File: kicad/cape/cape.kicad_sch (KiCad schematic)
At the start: 15 parts, among them M1 Motor_Servo_Feedback, M2 Motor_Servo_Feedback, P8 BeagleBone_Black_Header, P9 BeagleBone_Black_Header, U1 BNO055, U2 S13V20F5

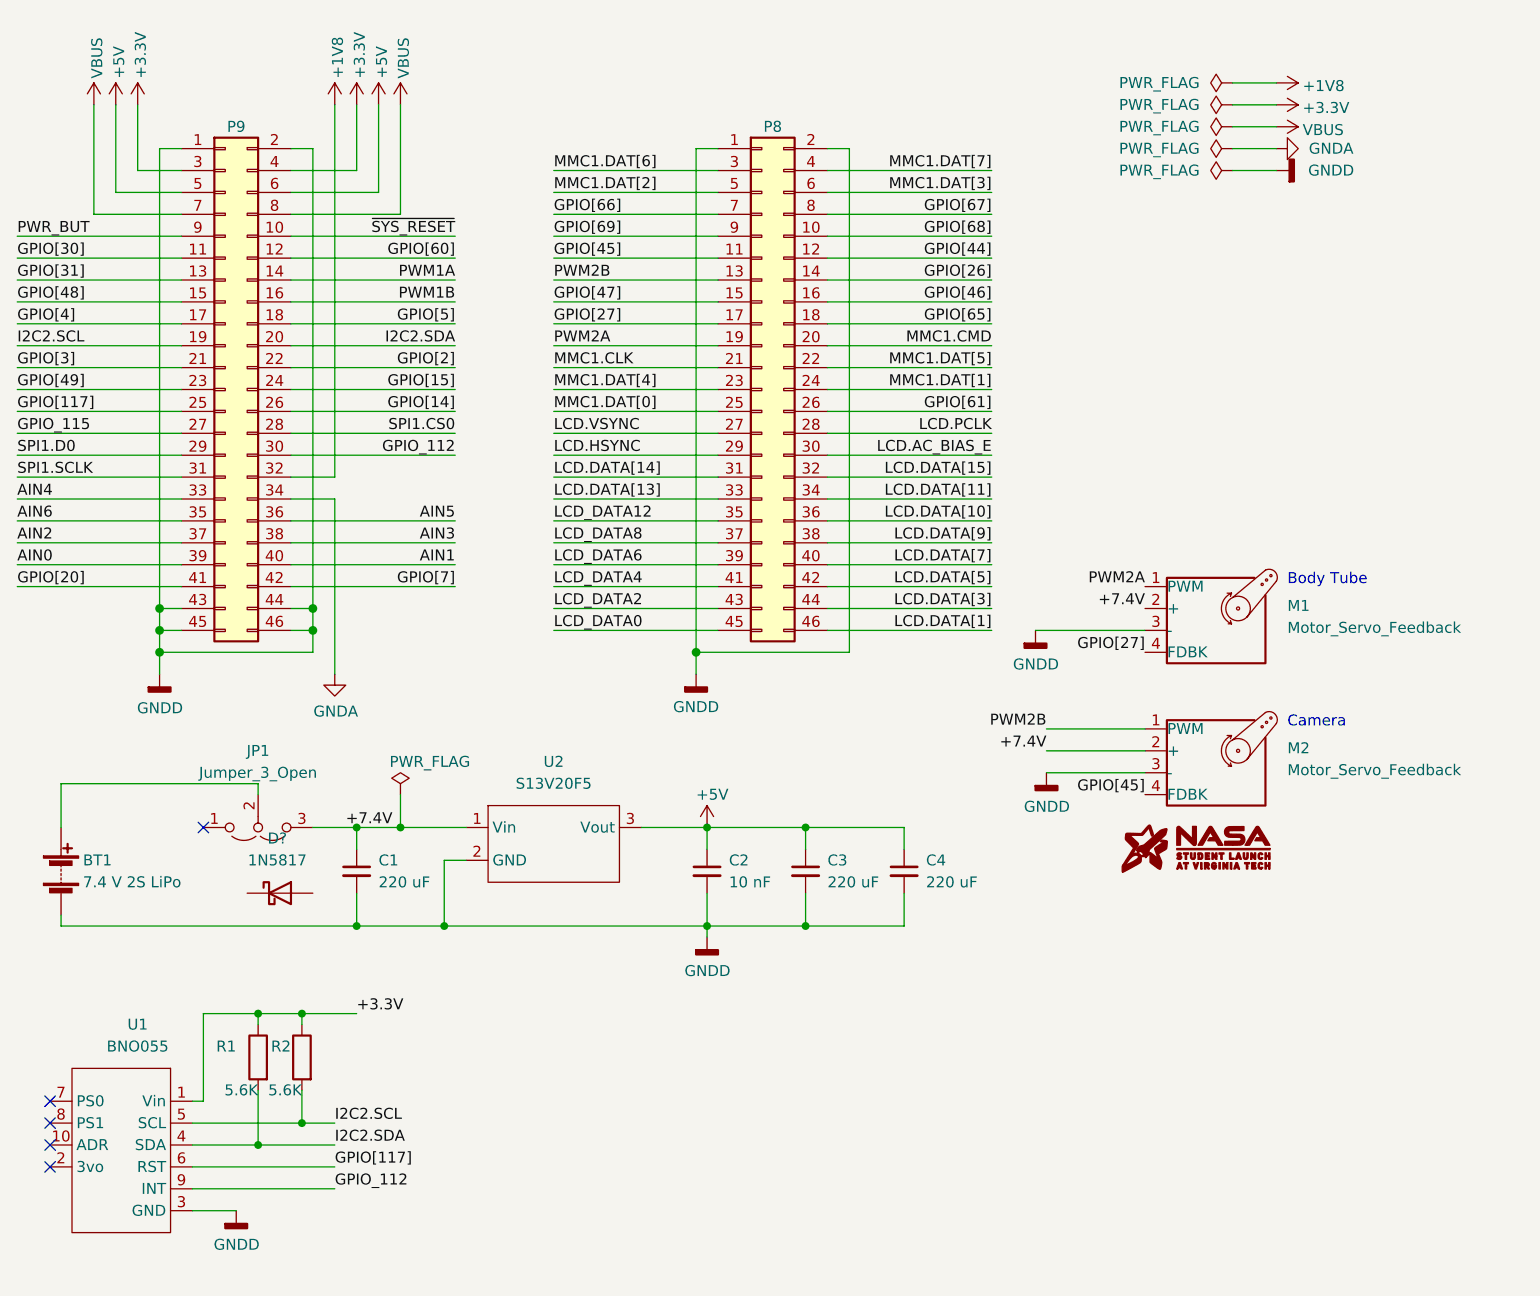
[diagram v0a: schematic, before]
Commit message: Finished schematic v1-5
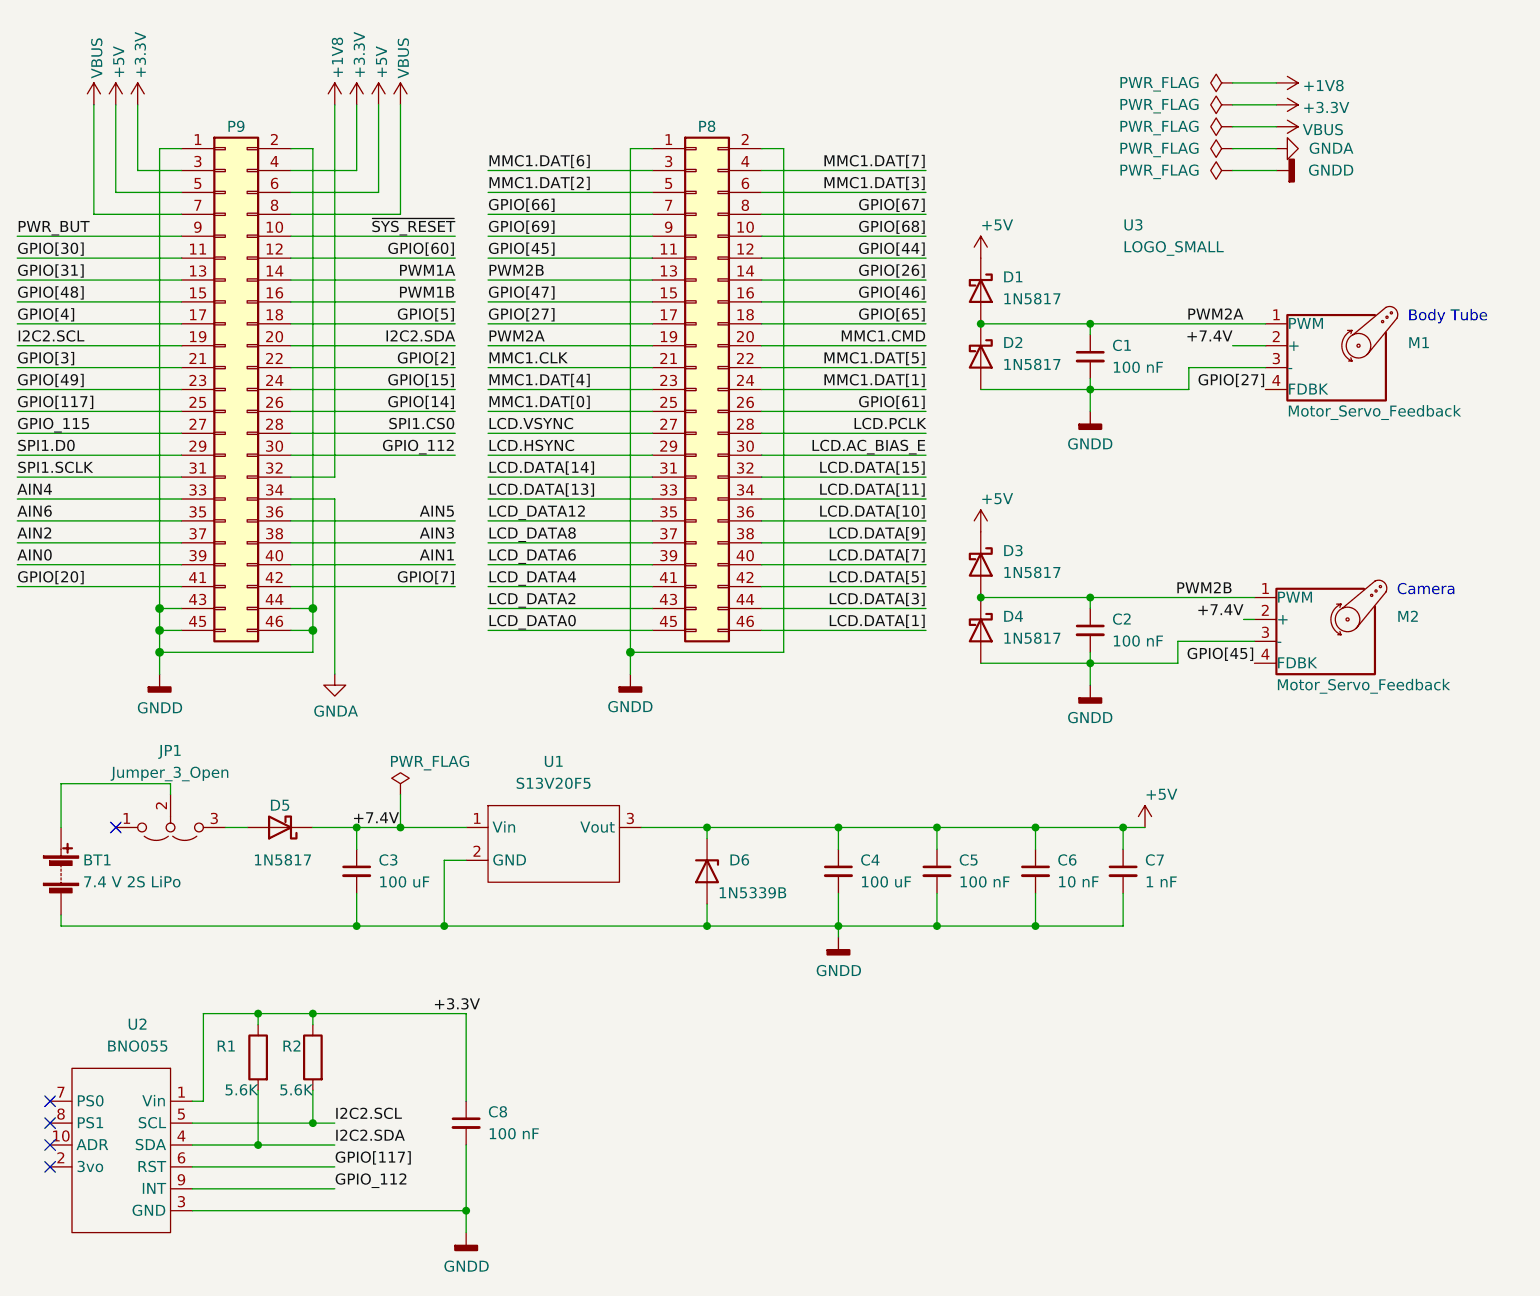
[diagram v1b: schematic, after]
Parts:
- removed C3: 220 uF, Capacitor_THT:C_Radial_D8.0mm_H7.0mm_P3.50mm, symbol Device:C_Small
- added C1, C2, C8: 100 nF, Capacitor_THT:C_Disc_D4.7mm_W2.5mm_P5.00mm, symbol Device:C_Small
- added C6: 10 nF, Capacitor_THT:C_Disc_D4.7mm_W2.5mm_P5.00mm, symbol Device:C_Small
- added C7: 1 nF, Capacitor_THT:C_Disc_D4.7mm_W2.5mm_P5.00mm, symbol Device:C_Small
- added D1, D2, D3, D4: 1N5817, Diode_THT:D_DO-41_SOD81_P10.16mm_Horizontal, symbol Diode:1N5817
- added D6: 1N5339B, Diode_THT:D_DO-201_P15.24mm_Horizontal, symbol Diode:1N53xxB
- added U3: LOGO_SMALL, payload_footprint_library:logo, symbol payload_logo:LOGO_SMALL
- BT1: footprint Connector_PinHeader_2.54mm:PinHeader_2x01_P2.54mm_Vertical -> Connector_PinHeader_2.54mm:PinHeader_2x01_P2.54mm_Horizontal
- C3: renamed from C1; value 220 uF -> 100 uF
- C4: renamed from C2; value 10 nF -> 100 uF; footprint Capacitor_THT:C_Disc_D10.0mm_W2.5mm_P5.00mm -> Capacitor_THT:C_Radial_D8.0mm_H7.0mm_P3.50mm
- C5: renamed from C4; value 220 uF -> 100 nF; footprint Capacitor_THT:C_Radial_D8.0mm_H7.0mm_P3.50mm -> Capacitor_THT:C_Disc_D4.7mm_W2.5mm_P5.00mm
- gave numbers to parts that had none: 1
- renumbered U2 to U1, U1 to U2
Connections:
- net +3.3V: now also C8.1
- net +5V: now also C6.1, C7.1, D1.1 (K), D3.1 (K), D6.1 (K)
- net +7.4V: now also D5.1 (K); no longer JP1.3 (B)
- net GNDD: now also C1.2, C2.2, C6.2, C7.2, C8.2, D2.2 (A), D4.2 (A), D6.2 (A)
- net PWM2A: now also C1.1, D1.2 (A), D2.1 (K)
- net PWM2B: now also C2.1, D3.2 (A), D4.1 (K)
- net at D5.2 (A): now also JP1.3 (B)
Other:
- moved on the sheet: C4, C5, D5, JP1, M1, M2, P8, R2

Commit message: Finished cape v1-5
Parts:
- added R3, R4: 1K, Resistor_THT:R_Axial_DIN0207_L6.3mm_D2.5mm_P15.24mm_Horizontal, symbol Device:R
- BT1: footprint Connector_PinHeader_2.54mm:PinHeader_2x01_P2.54mm_Horizontal -> Connector_PinHeader_2.54mm:PinHeader_2x01_P2.54mm_Vertical
- M1, M2: footprint Connector_PinHeader_2.54mm:PinHeader_1x04_P2.54mm_Vertical -> payload_footprint_library:FeedbackServo
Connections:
- net PWM2A: now also R3.1; no longer C1.1, M1.1 (PWM)
- net PWM2B: now also R4.1; no longer C2.1, M2.1 (PWM)
- net batt: now reaches BT1.1 (+), JP1.2 (C)
- new net: C1.1, M1.1 (PWM), R3.2
- new net: C2.1, M2.1 (PWM), R4.2
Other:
- moved on the sheet: C1, C2, D1, D2, D3, D4, M2
